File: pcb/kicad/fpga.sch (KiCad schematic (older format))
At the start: 1 part, among them U4 XC3S400-PQ208

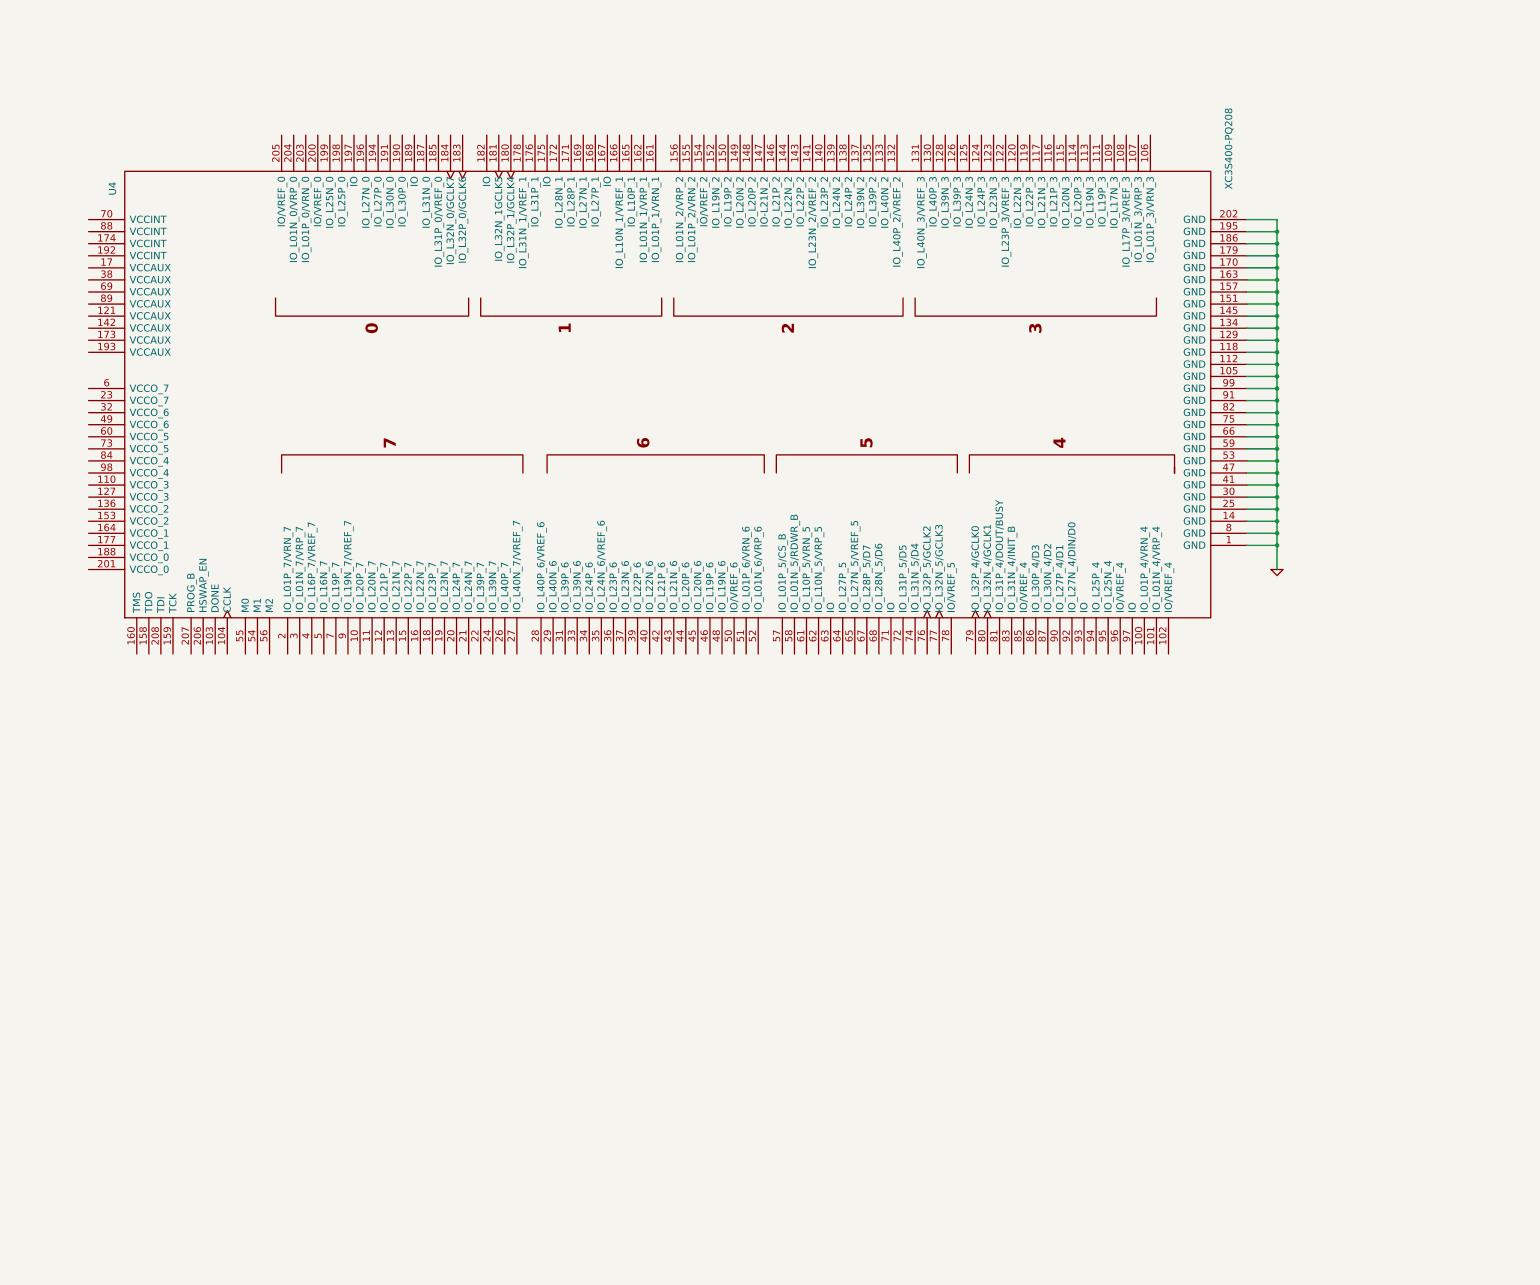
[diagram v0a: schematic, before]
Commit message: clean up AVR code(deprecated), kicad libs, pcb WIP
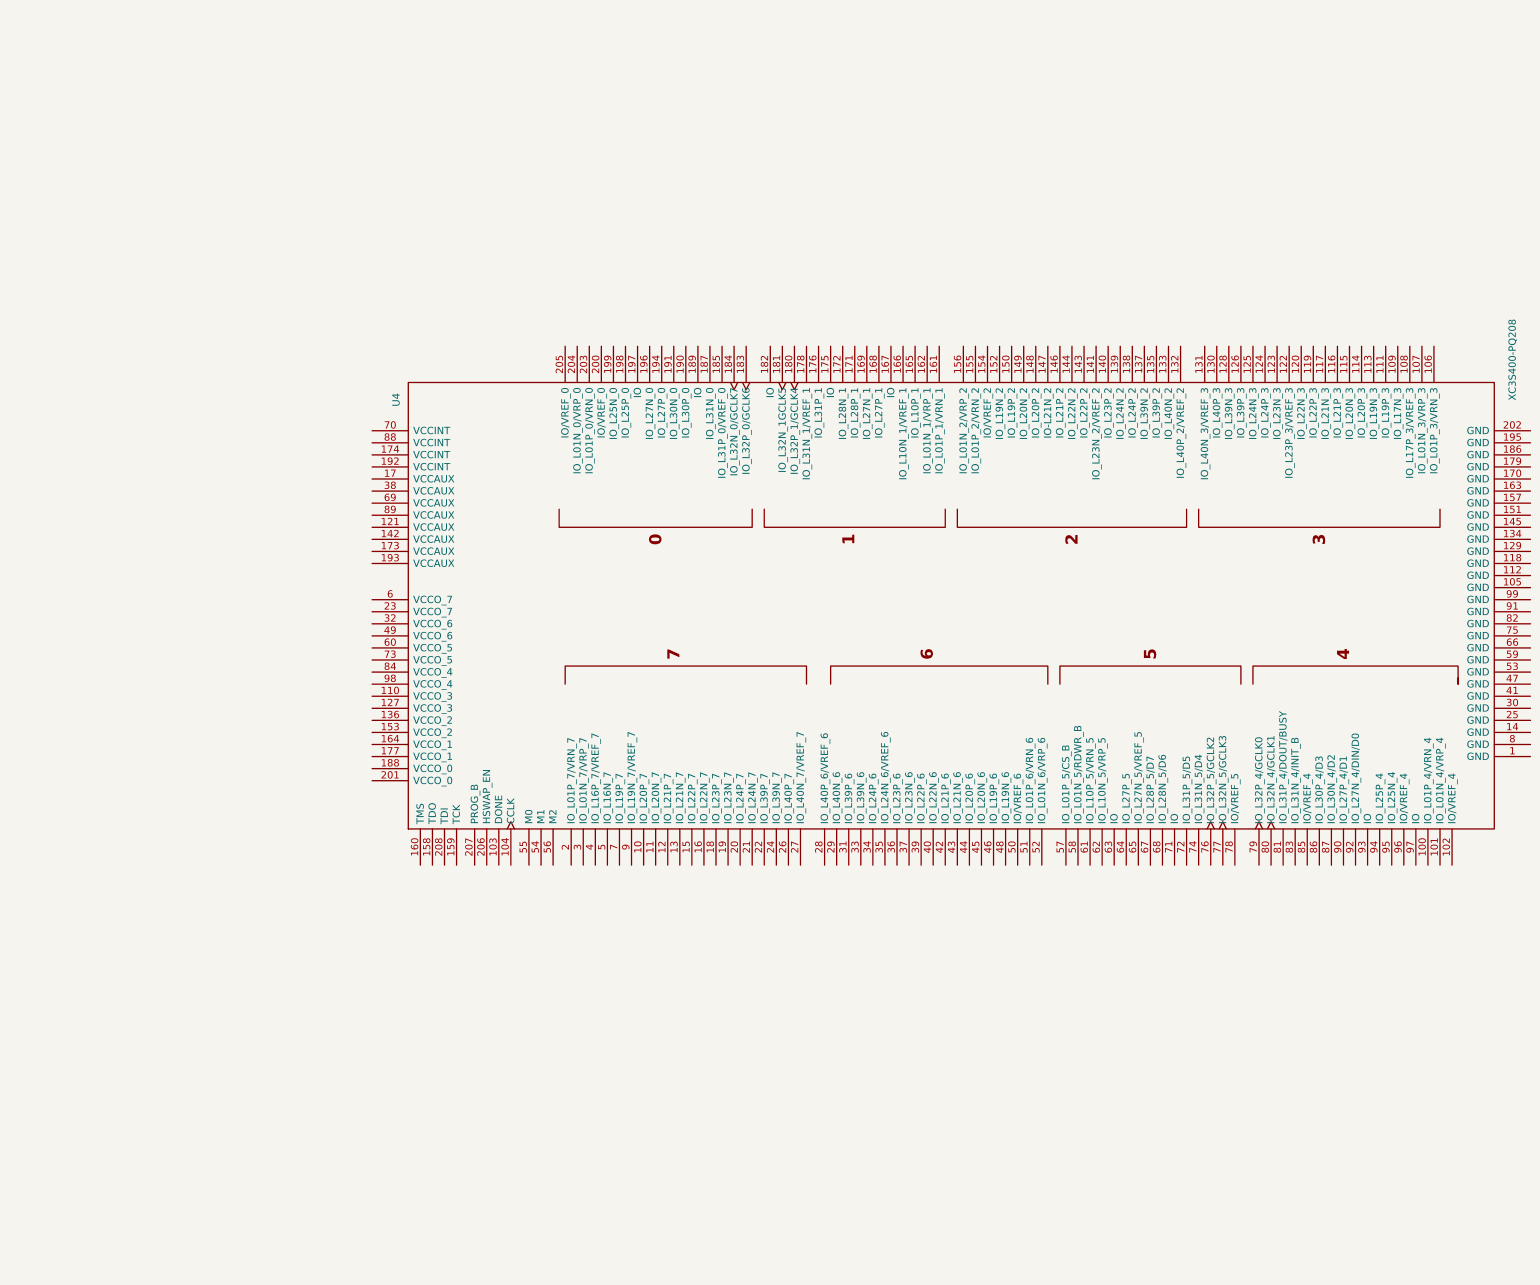
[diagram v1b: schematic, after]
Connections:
- removed net GND: U4.1 (GND), U4.105 (GND), U4.112 (GND), U4.118 (GND), U4.129 (GND), U4.134 (GND), U4.14 (GND), U4.145 (GND), U4.151 (GND), U4.157 (GND), U4.163 (GND), U4.170 (GND), U4.179 (GND), U4.186 (GND), U4.195 (GND), U4.202 (GND), U4.25 (GND), U4.30 (GND), U4.41 (GND), U4.47 (GND), U4.53 (GND), U4.59 (GND), U4.66 (GND), U4.75 (GND), U4.8 (GND), U4.82 (GND), U4.91 (GND), U4.99 (GND)
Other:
- moved on the sheet: U4
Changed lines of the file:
@@
-EESchema Schematic File Version 2  date Tue 09 Feb 2010 11:25:34 PM CET
+EESchema Schematic File Version 2  date Wed 24 Mar 2010 11:33:24 PM CET
 LIBS:sd2snes-cache
 LIBS:power
@@
 LIBS:lpc1754
 LIBS:sdcard
-LIBS:testsw
+LIBS:sd_card
+LIBS:cy62148ev30
+LIBS:mt45w8mw16
+LIBS:cs4344
 EELAYER 24  0
 EELAYER END
-$Descr A4 11700 8267
-Sheet 3 5
+$Descr A3 16535 11700
+Sheet 4 6
 Title ""
 Date "9 feb 2010"
@@
 Comment4 ""
 $EndDescr
-Connection ~ 11050 2500
-Wire Wire Line
-	10800 2500 11050 2500
-Connection ~ 11050 2700
-Wire Wire Line
-	10800 2700 11050 2700
-Connection ~ 11050 2900
-Wire Wire Line
-	10800 2900 11050 2900
-Connection ~ 11050 3100
-Wire Wire Line
-	10800 3100 11050 3100
-Connection ~ 11050 3300
-Wire Wire Line
-	10800 3300 11050 3300
-Connection ~ 11050 3500
-Wire Wire Line
-	10800 3500 11050 3500
-Connection ~ 11050 3700
-Wire Wire Line
-	10800 3700 11050 3700
-Connection ~ 11050 3900
-Wire Wire Line
-	10800 3900 11050 3900
-Connection ~ 11050 4100
-Wire Wire Line
-	10800 4100 11050 4100
-Connection ~ 11050 4300
-Wire Wire Line
-	10800 4300 11050 4300
-Connection ~ 11050 4500
-Wire Wire Line
-	10800 4500 11050 4500
-Connection ~ 11050 4700
-Wire Wire Line
-	10800 4700 11050 4700
-Connection ~ 11050 4900
-Wire Wire Line
-	10800 4900 11050 4900
-Connection ~ 11050 5100
-Wire Wire Line
-	10800 5100 11050 5100
-Wire Wire Line
-	10800 2400 11050 2400
-Wire Wire Line
-	11050 2400 11050 5300
-Wire Wire Line
-	11050 5000 10800 5000
-Connection ~ 11050 5000
-Wire Wire Line
-	11050 4800 10800 4800
-Connection ~ 11050 4800
-Wire Wire Line
-	11050 4600 10800 4600
-Connection ~ 11050 4600
-Wire Wire Line
-	11050 4400 10800 4400
-Connection ~ 11050 4400
-Wire Wire Line
-	11050 4200 10800 4200
-Connection ~ 11050 4200
-Wire Wire Line
-	11050 4000 10800 4000
-Connection ~ 11050 4000
-Wire Wire Line
-	11050 3800 10800 3800
-Connection ~ 11050 3800
-Wire Wire Line
-	11050 3600 10800 3600
-Connection ~ 11050 3600
-Wire Wire Line
-	11050 3400 10800 3400
-Connection ~ 11050 3400
-Wire Wire Line
-	11050 3200 10800 3200
-Connection ~ 11050 3200
-Wire Wire Line
-	11050 3000 10800 3000
-Connection ~ 11050 3000
-Wire Wire Line
-	11050 2800 10800 2800
-Connection ~ 11050 2800
-Wire Wire Line
-	11050 2600 10800 2600
-Connection ~ 11050 2600
-$Comp
-L GND #PWR013
-U 1 1 4B6ED488
-P 11050 5300
-F 0 "#PWR013" H 11050 5300 30  0001 C CNN
-F 1 "GND" H 11050 5230 30  0001 C CNN
-	1    11050 5300
-	1    0    0    -1
-$EndComp
 $Comp
 L XC3S400-PQ208 U4
 U 1 1 4B6E1931
-P 6000 3850
-F 0 "U4" H 7650 8450 60  0000 L CNN
-F 1 "XC3S400-PQ208" H 7700 -800 60  0000 L CNN
-	1    6000 3850
+P 8350 5600
+F 0 "U4" H 10000 10200 60  0000 L CNN
+F 1 "XC3S400-PQ208" H 10050 950 60  0000 L CNN
+	1    8350 5600
 	0    -1   -1   0
 $EndComp

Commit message: kicad wip
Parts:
- added C18, C19, C20, C21, C22, C23, C24, C25, C26, C27, C28, C29, C30, C31: 100n, symbol C
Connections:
- net labels added: +1.2V, +2.5V, +3.3V, GND
- wire segments 0 -> 114
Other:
- note added: "JTAG"
- note added: "SPM"
- moved on the sheet: U4

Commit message: Schematics+PCB WIP
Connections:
- net labels added: DAC_LRCK, DAC_MCLK, DAC_SDIN, DATABUS_/OE, DATABUS_DIR, DIN, FPGA_CLK, INIT_B, IRQ_DIR, MCU_SPI_MISO, MCU_SPI_MOSI, MCU_SPI_SCK, MCU_SPI_SS, SD_SPI_MISO, SD_SPI_MOSI, SD_SPI_SCK, SD_SPI_SS, SNES_/IRQ, SNES_/PARD, SNES_/PAWR, SNES_/RD, SNES_/ROMSEL, SNES_/WR, SNES_A0, SNES_A1, SNES_A10, SNES_A11, SNES_A12, SNES_A13, SNES_A14, SNES_A15, SNES_A16, SNES_A17, SNES_A18, SNES_A19, SNES_A2, SNES_A20, SNES_A21, SNES_A22, SNES_A23, SNES_A3, SNES_A4, SNES_A5, SNES_A6, SNES_A7, SNES_A8, SNES_A9, SNES_CPU_CLK, SNES_D0, SNES_D1, SNES_D2, SNES_D3, SNES_D4, SNES_D5, SNES_D6, SNES_D7, SNES_PA0, SNES_PA1, SNES_PA2, SNES_PA3, SNES_PA4, SNES_PA5, SNES_PA6, SNES_PA7, SNES_REFRESH, SNES_SYS_CLK
- wire segments 114 -> 168
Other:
- note removed: "SPM"

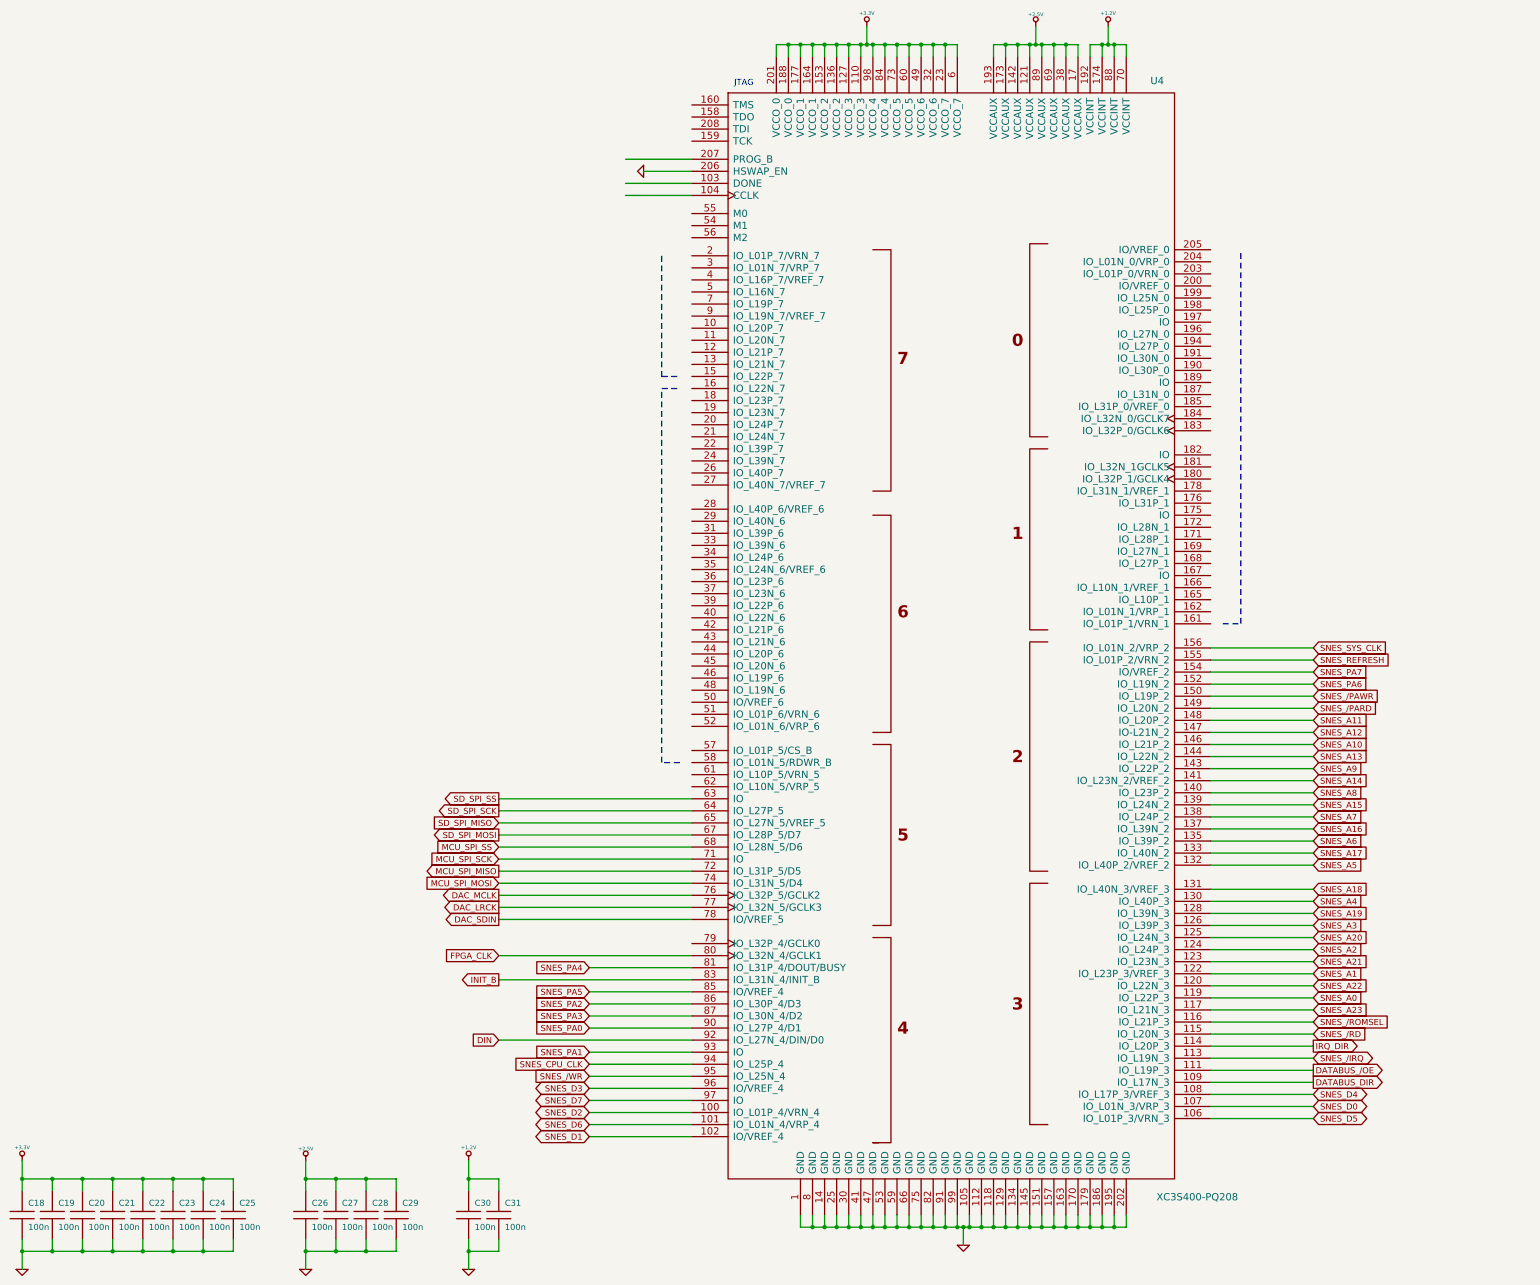
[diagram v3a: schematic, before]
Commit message: Schematics: connect PSRAM
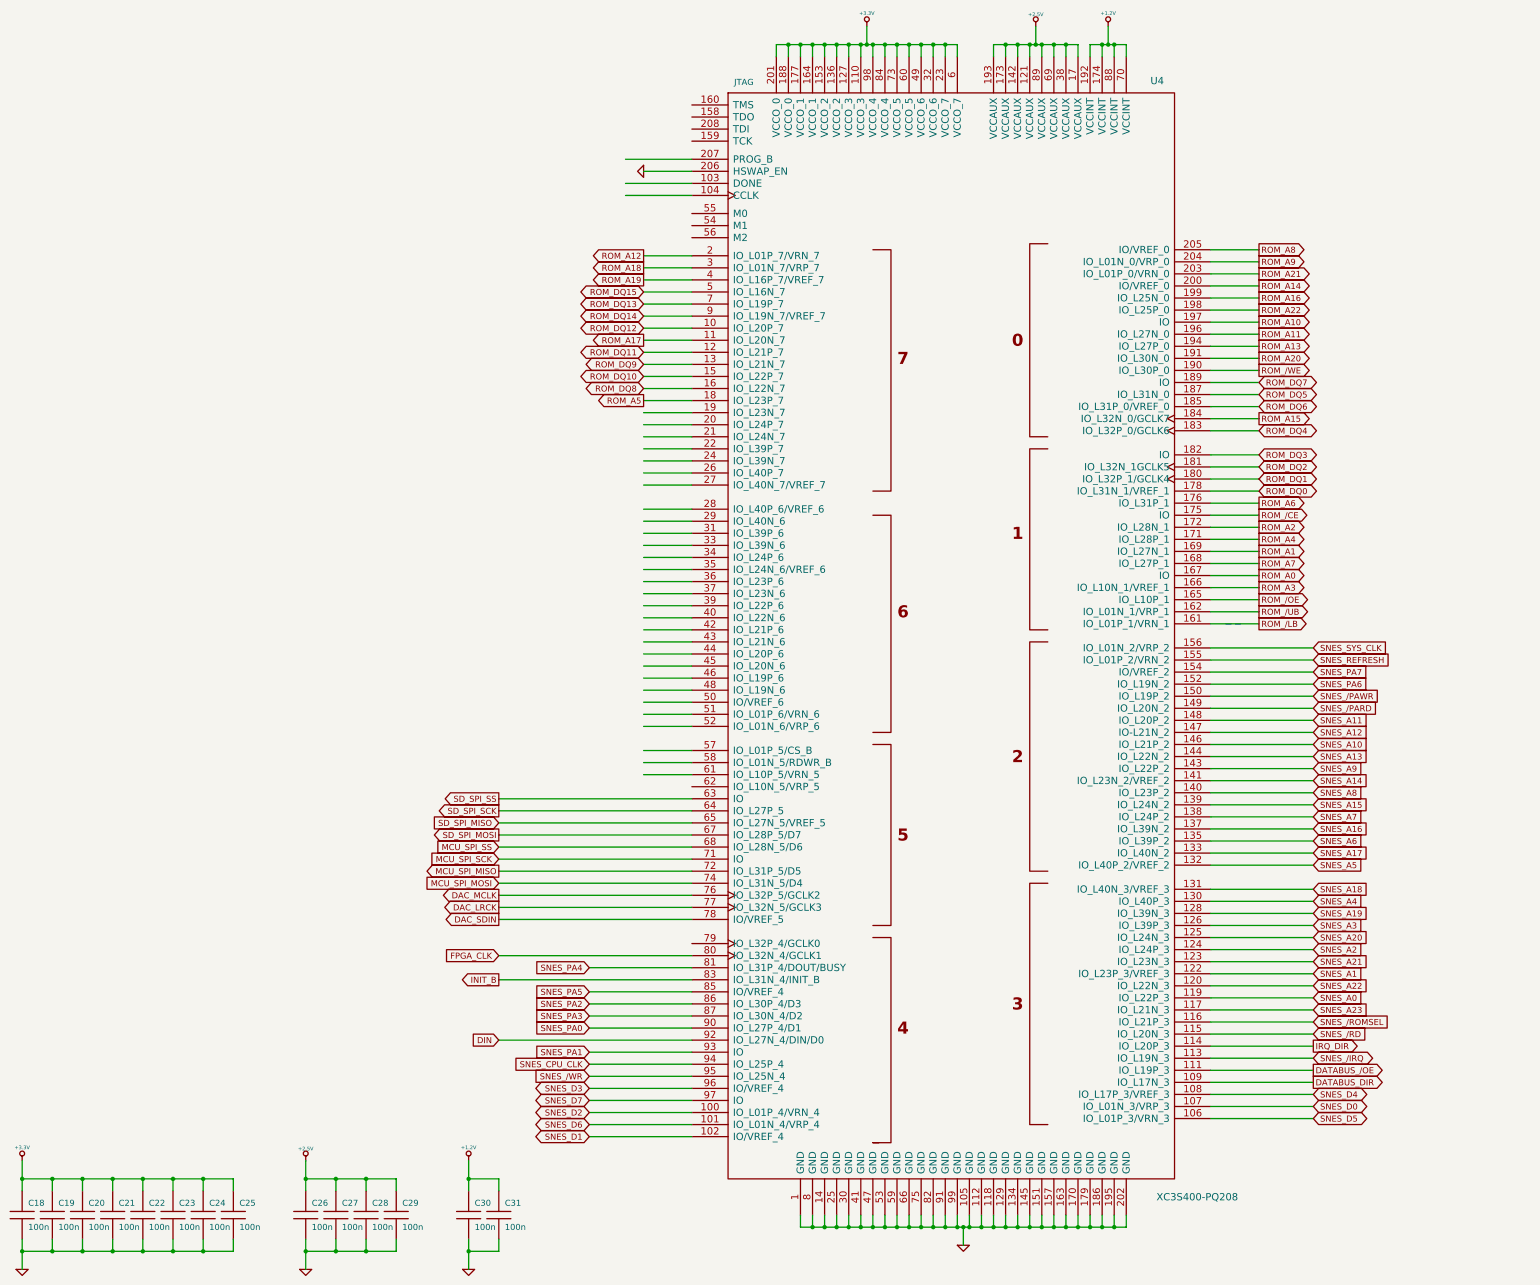
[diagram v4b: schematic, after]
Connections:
- net labels added: ROM_/CE, ROM_/LB, ROM_/OE, ROM_/UB, ROM_/WE, ROM_A0, ROM_A1, ROM_A10, ROM_A11, ROM_A12, ROM_A13, ROM_A14, ROM_A15, ROM_A16, ROM_A17, ROM_A18, ROM_A19, ROM_A2, ROM_A20, ROM_A21, ROM_A22, ROM_A3, ROM_A4, ROM_A5, ROM_A6, ROM_A7, ROM_A8, ROM_A9, ROM_DQ0, ROM_DQ1, ROM_DQ10, ROM_DQ11, ROM_DQ12, ROM_DQ13, ROM_DQ14, ROM_DQ15, ROM_DQ2, ROM_DQ3, ROM_DQ4, ROM_DQ5, ROM_DQ6, ROM_DQ7, ROM_DQ8, ROM_DQ9
- wire segments 168 -> 241

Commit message: pcb wip
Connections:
- net labels added: DIN+MCU_/OVR, INIT_B+MCU_/IRQ
- net labels removed: DIN, INIT_B

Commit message: pcb wip
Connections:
- net labels added: RAM_/OE, RAM_/WE, RAM_A0, RAM_A1, RAM_A10, RAM_A11, RAM_A12, RAM_A13, RAM_A14, RAM_A15, RAM_A16, RAM_A17, RAM_A18, RAM_A2, RAM_A3, RAM_A4, RAM_A5, RAM_A6, RAM_A7, RAM_A8, RAM_A9, RAM_DQ0, RAM_DQ1, RAM_DQ2, RAM_DQ3, RAM_DQ4, RAM_DQ5, RAM_DQ6, RAM_DQ7
